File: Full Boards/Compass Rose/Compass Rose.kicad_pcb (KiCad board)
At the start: 4 copper layers, 170 x 180 mm, 245 parts, among them J1 Program Header, Q10 2N3904, Q11 AO3401A, Q12 2N3904, Q7 AO3401A, Q8 2N3904, Q9 AO3401A, SW1 SW_MEC_5G, SW2 SW_MEC_5G, U1 ISO1044BD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

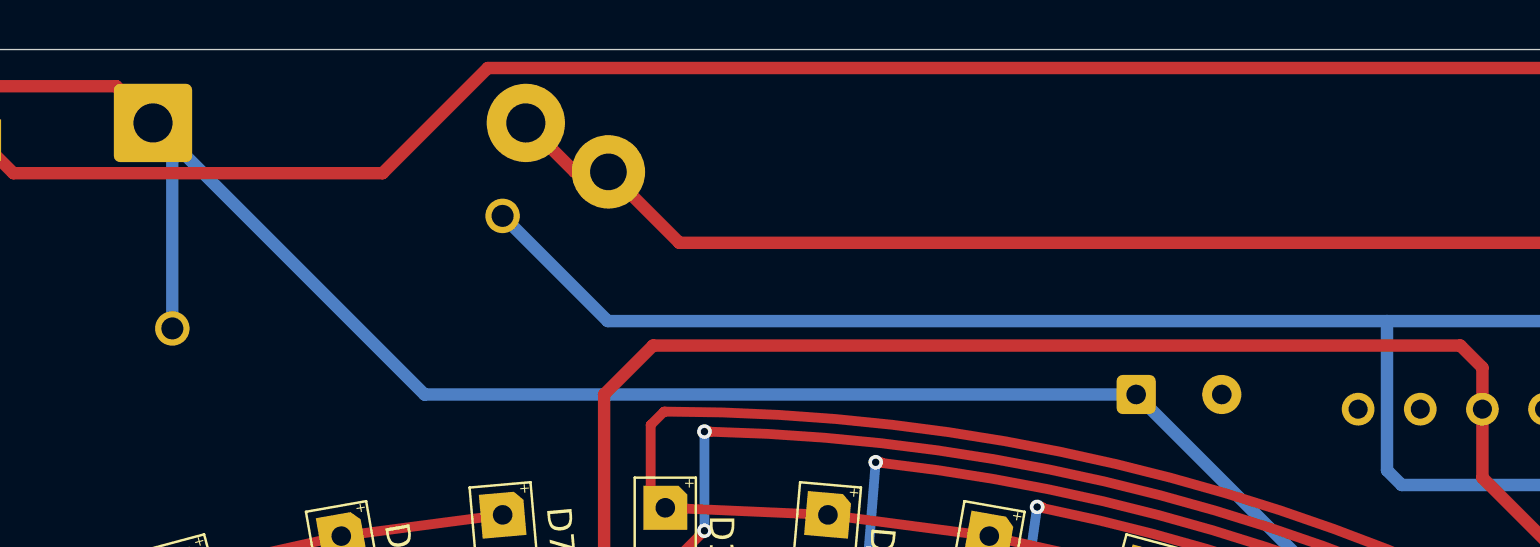
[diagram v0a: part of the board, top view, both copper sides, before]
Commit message: Updated PCBs to swap RVS diodes from SLD15-018 to SLD22-018. Also swapped out the inductor from 7847111100 to PA4340.103NLT.
Signed-off-by: Madison Kelly <digital.mermaid@gmail.com>
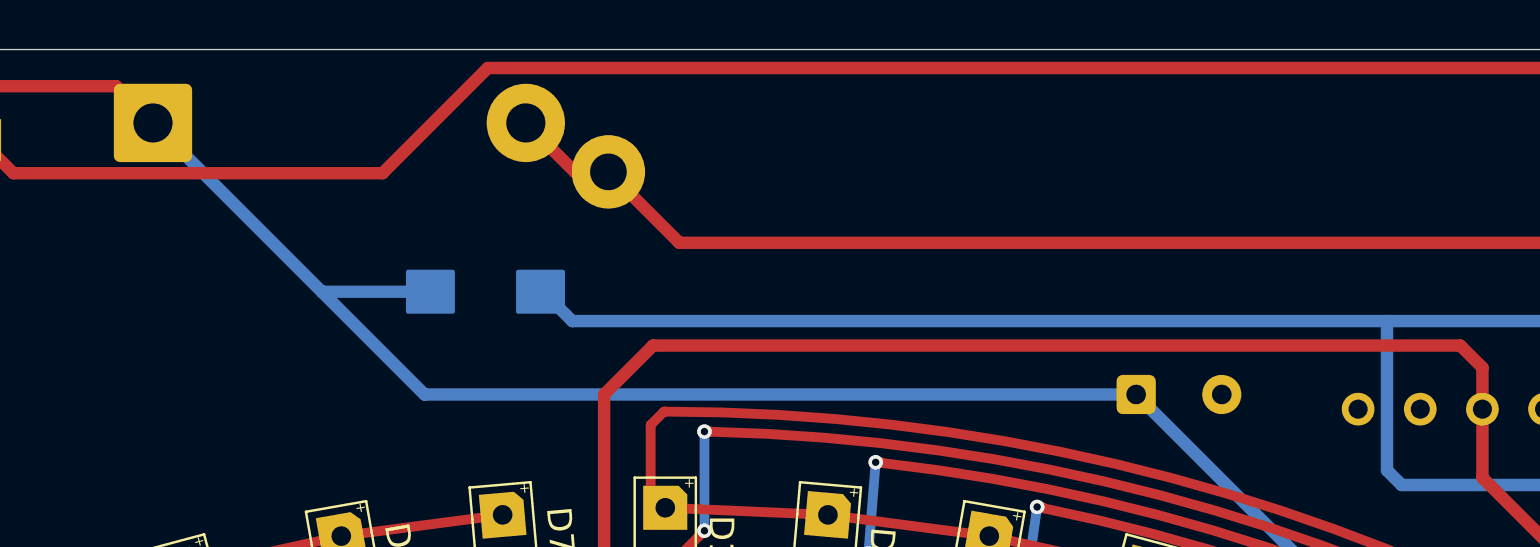
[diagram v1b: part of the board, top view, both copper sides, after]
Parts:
- removed L2: 7847111100, mr-stuff:WE-RCIT_7847111100
- added L1: PA4340.103NLT, mr-stuff:Pulse PA4340.103NLT, B.Cu at (173.7, 53.9)
- D146: value SLD15-018 -> SLD22-018
- renumbered N2K2 to N2K1
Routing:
- net V_RAW: track 128.6 -> 124.3 mm
- net Net-(PS2-+VIN): track 76.0 -> 73.2 mm

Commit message: Updated boards and schematics.
These are the version that have been ordered. Any further changes will be a new version.

Signed-off-by: Madison Kelly <digital.mermaid@gmail.com>
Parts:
- removed D147, D148, D149, D150, D151, D152: 1N5822, Diode_THT:D_DO-41_SOD81_P10.16mm_Horizontal
- added C25: 0.1uF, mr-stuff:RCE5C1H104J2A2H03B, B.Cu at (167.5, 178.5)
- added C26: 0.1uF, mr-stuff:RCE5C1H104J2A2H03B, B.Cu at (207.2, 178.6)
- added C27: 0.1uF, mr-stuff:RCE5C1H104J2A2H03B, B.Cu at (241.5, 206.1)
- added J2: Future Bonding, Connector_PinHeader_2.54mm:PinHeader_1x03_P2.54mm_Vertical, B.Cu at (235.8, 72.5)
- added R23: 3.3K, Resistor_THT:R_Axial_DIN0207_L6.3mm_D2.5mm_P7.62mm_Horizontal, B.Cu at (145.1, 104.6)
- added R24: 3.3K, Resistor_THT:R_Axial_DIN0207_L6.3mm_D2.5mm_P7.62mm_Horizontal, B.Cu at (145.1, 101.5)
- added R25: 3.3K, Resistor_THT:R_Axial_DIN0207_L6.3mm_D2.5mm_P7.62mm_Horizontal, B.Cu at (131.2, 124.1)
- added R26: 3.3K, Resistor_THT:R_Axial_DIN0207_L6.3mm_D2.5mm_P7.62mm_Horizontal, B.Cu at (131.2, 127.2)
- C7: value TDK FA28NP01H152JNU06 -> 0.1uF; footprint mr-stuff:TDK CAPRB500W50L400T250H550 -> mr-stuff:RCE5C1H104J2A2H03B
- R21, R22, R68: value 10 -> 475
- moved TVS3 10.4 mm to (236.3, 205.5)
- moved C7 5.18 mm to (227.4, 70.2)
- moved TVS1 3.75 mm to (164.9, 177.4), turned to 90 degrees
- moved TVS2 3.71 mm to (204.6, 177.4), turned to -90 degrees
- moved C6 2.00 mm to (226.8, 67.0)
- moved DE2 0.18 mm to (235.1, 214.3)
- moved DE1 0.16 mm to (128.0, 53.6)
- moved C13 0.14 mm to (114.4, 68.9)
- moved C12 0.14 mm to (112.6, 59.9)
- moved C21 0.14 mm to (179.3, 90.8)
- moved N2K1 0.13 mm to (240.2, 51.1)
- moved C10 0.10 mm to (122.2, 65.4)
- moved C20 0.10 mm to (182.6, 90.8)
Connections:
- C7 pad 1: GND -> GND_SHIP
- C7 pad 2: GND_SHIP -> GND
- N2K1 pad 1: unconnected-(N2K1-Shield-Pad1) -> Net-(J2-Pin_1)
- U3 pad 10: unconnected-(U3-T2IN-Pad10) -> +3.3V
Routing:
- net GND: track 150.4 -> 119.4 mm, vias 5 -> 4
- net Net-(J2-Pin_1): track 0.00 -> 29.3 mm, vias 0 -> 1
- net /BOARD_I2C_SDA: track 87.8 -> 116.9 mm
- net /BOARD_I2C_SCL: track 102.4 -> 129.1 mm
- net +5V: track 486.5 -> 476.7 mm
- net /IS31_I2C_SDA: track 59.3 -> 68.9 mm
- net +3.3V: track 107.6 -> 116.8 mm, vias 24 -> 25
- net GND_SHIP: track 600.8 -> 609.7 mm
- net /DISPLAY_ON_IN_PLUG: track 19.7 -> 25.1 mm
- net /CA8: track 404.2 -> 399.1 mm, vias 11 -> 10
- net /IS31_I2C_SCL: track 76.1 -> 80.6 mm
- net /LCD_PGDOWN_IN: track 123.6 -> 120.2 mm
- net /DISPLAY_ON_IN: track 143.1 -> 145.7 mm
- net V_RAW: track 124.3 -> 126.5 mm
- net /LCD_PGUP_IN_PLUG: track 90.9 -> 88.9 mm
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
